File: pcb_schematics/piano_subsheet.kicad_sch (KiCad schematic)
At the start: 19 parts, among them U1 SS49E

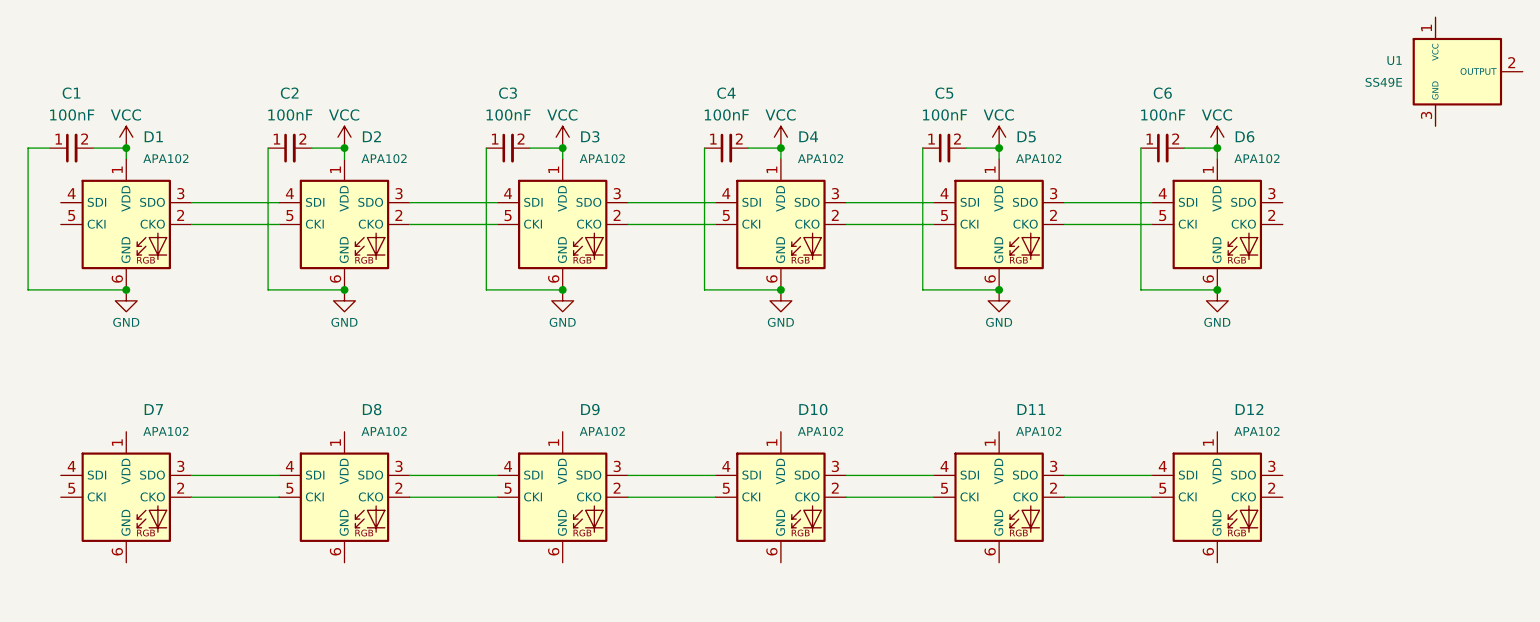
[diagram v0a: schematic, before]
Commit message: more symbols
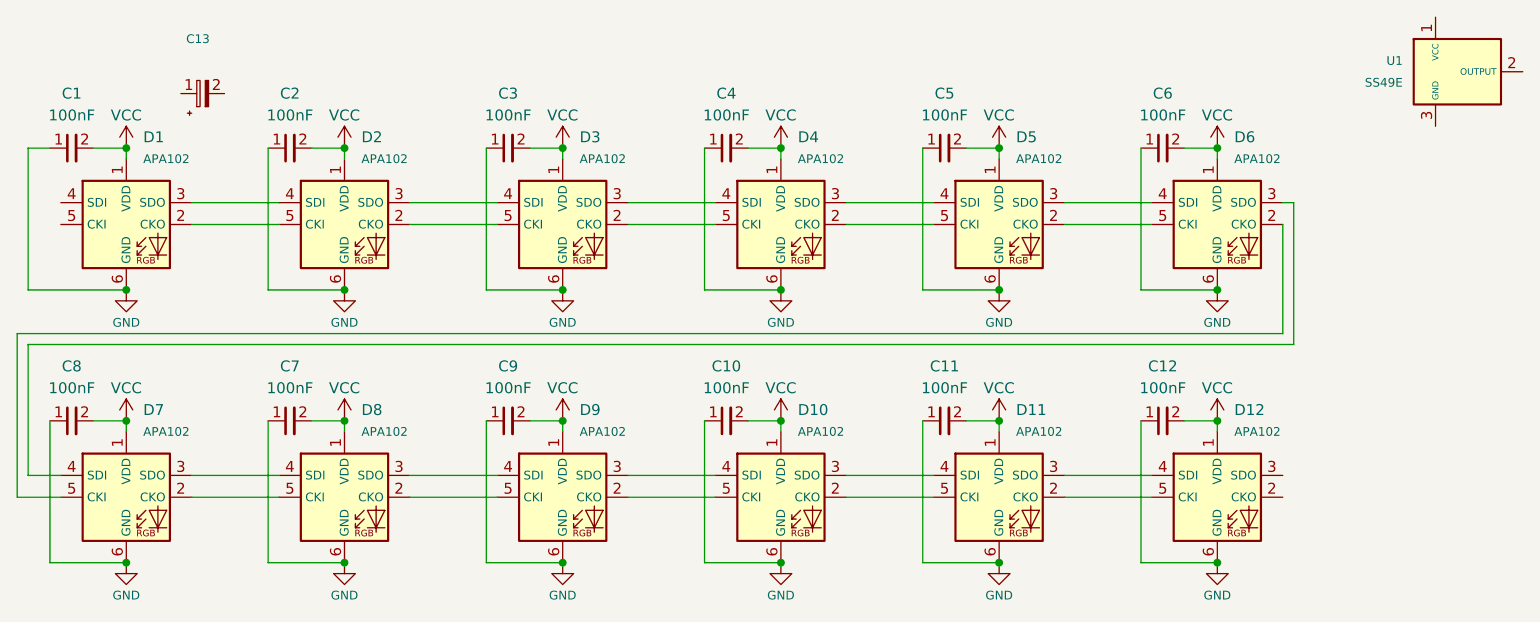
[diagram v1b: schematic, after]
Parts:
- added C10, C11, C12, C7, C8, C9: 100nF, symbol Symbols:Capacitor 0603
- added C13: ~, symbol Symbols:Capacitor Electrolytic
- C1, C2, C3, C4, C5, C6: symbol Symbols:Capacitor -> Symbols:Capacitor 0603
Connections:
- net GND: now also D10.6 (GND), D11.6 (GND), D12.6 (GND), D7.6 (GND), D8.6 (GND), D9.6 (GND), C10.1, C11.1, C12.1, C7.1, C8.1, C9.1
- net VCC: now also D10.1 (VDD), D11.1 (VDD), D12.1 (VDD), D7.1 (VDD), D8.1 (VDD), D9.1 (VDD), C10.2, C11.2, C12.2, C7.2, C8.2, C9.2
- net at D6.2 (CKO): now also D7.5 (CKI)
- net at D6.3 (SDO): now also D7.4 (SDI)
